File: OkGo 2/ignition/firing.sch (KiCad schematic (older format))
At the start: 62 parts, among them K201 RELAY_SPST, K202 RELAY_SPST, K203 RELAY_SPST, K204 RELAY_SPST, K205 RELAY_SPST, P201 CH1, P202 CH2, P203 CH3, P204 CH4, Q201 BSS138BK, Q202 BSS138BK, Q203 BSS138BK, Q204 BSS138BK, Q205 BSS138BK

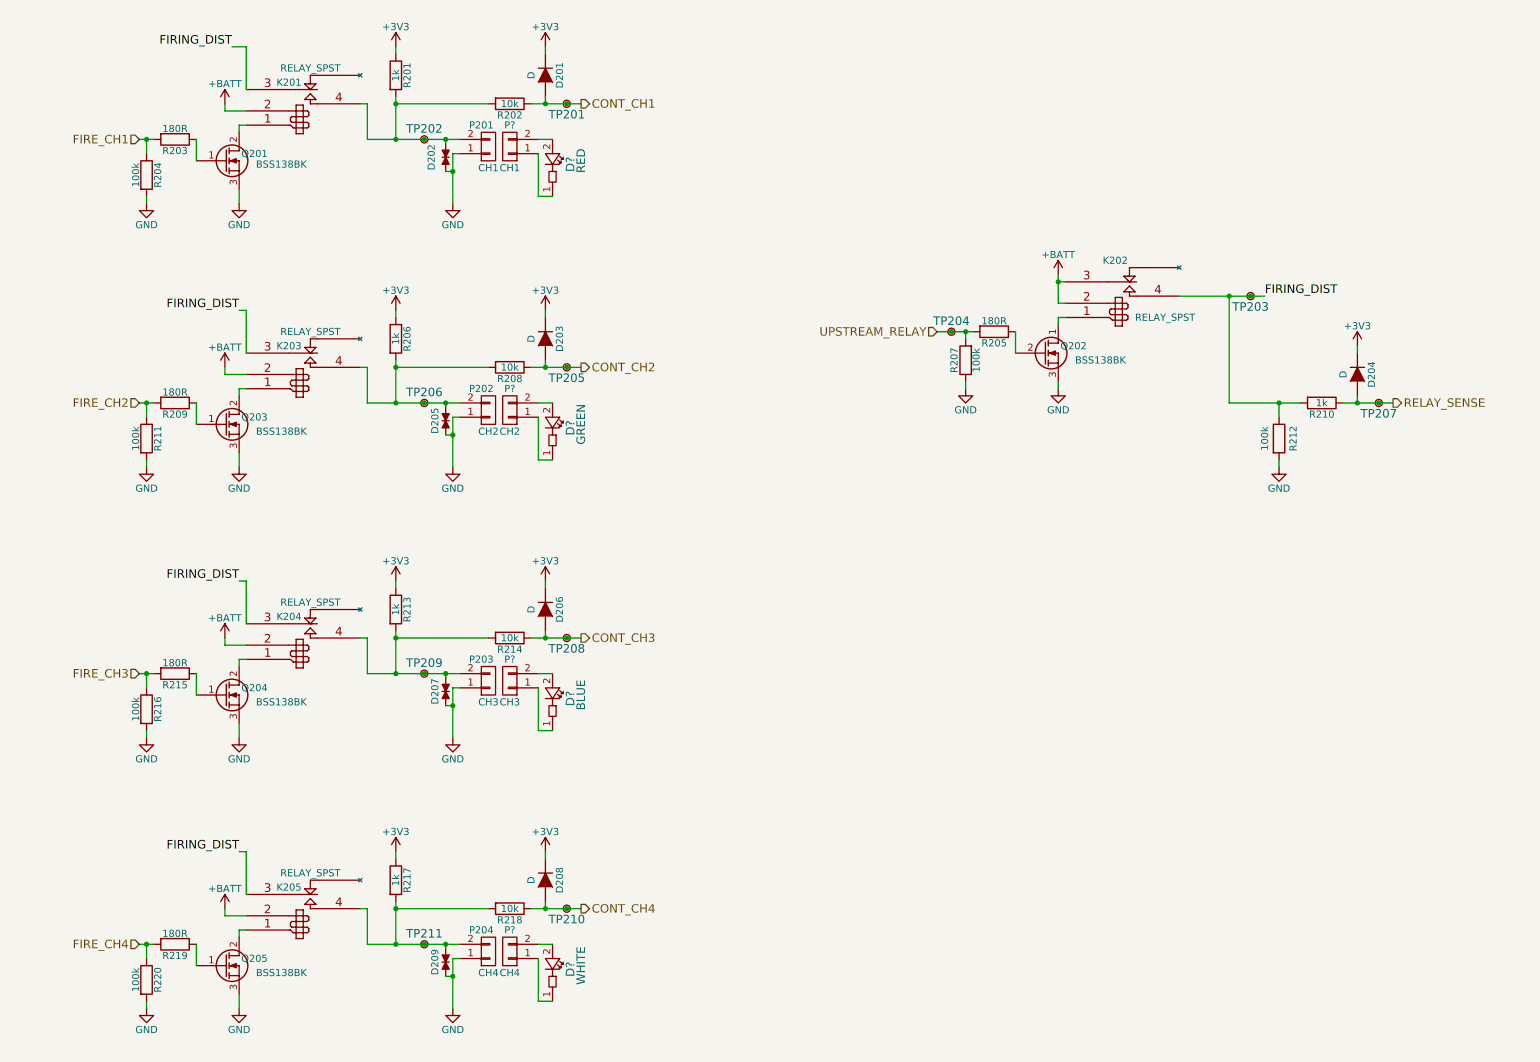
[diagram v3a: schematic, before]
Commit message: New power buttons and arm/disarm LED
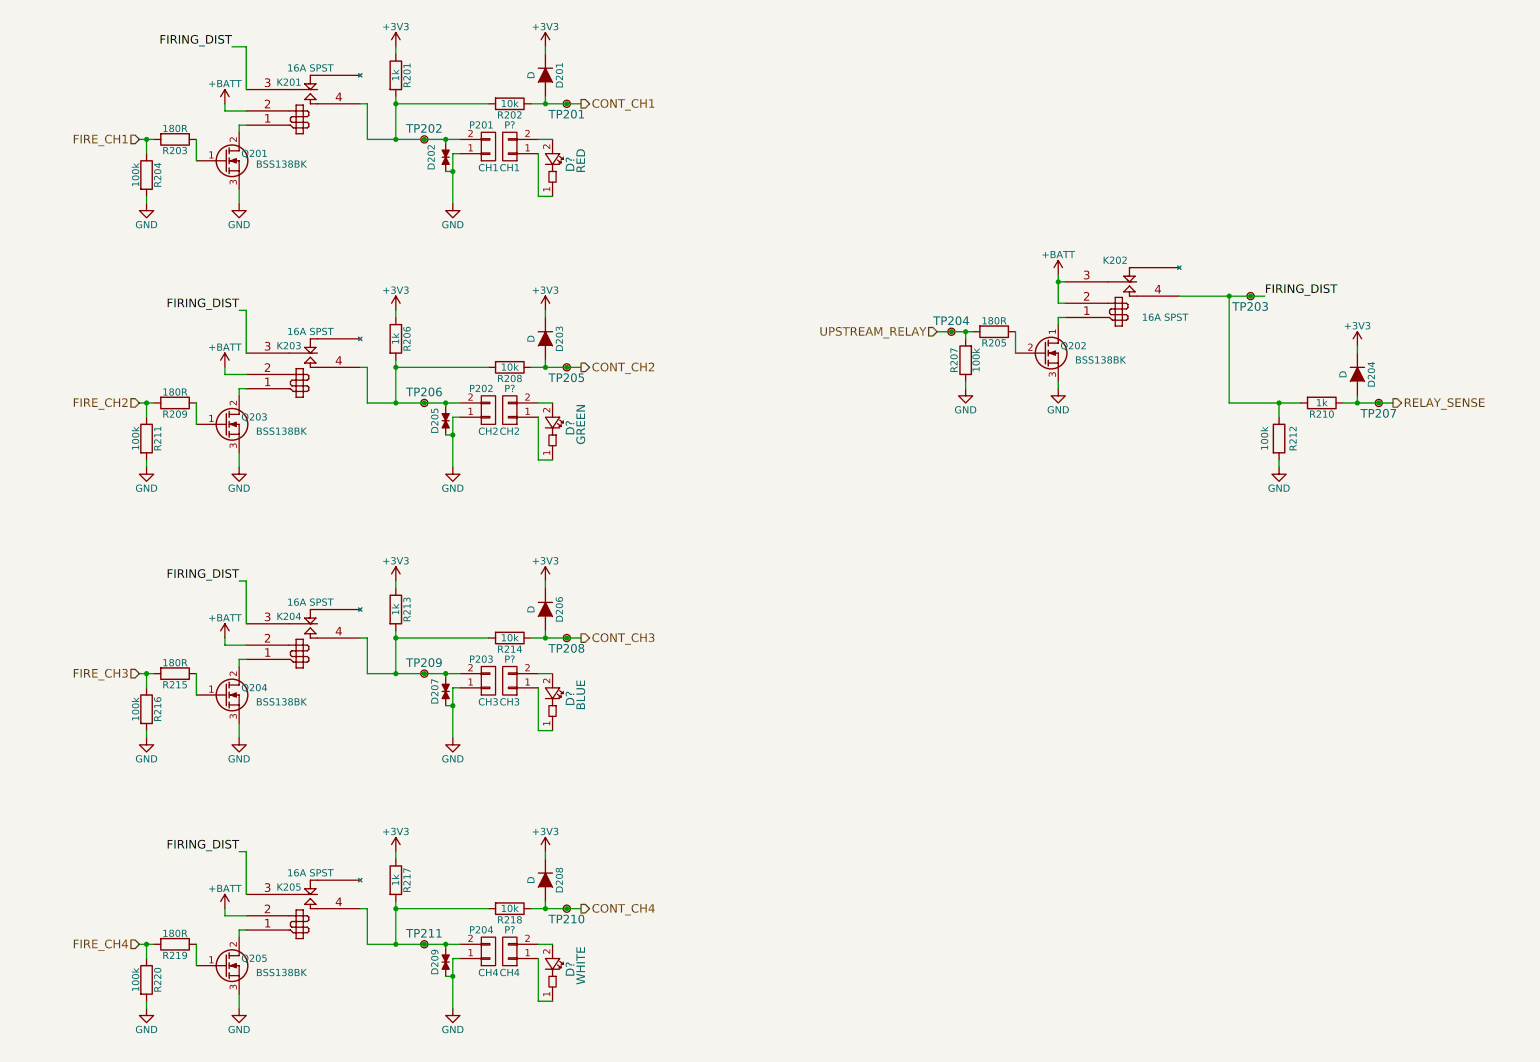
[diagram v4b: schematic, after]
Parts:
- K201, K202, K203, K204, K205: value RELAY_SPST -> 16A SPST
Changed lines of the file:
@@
 LIBS:lipo_3s
 LIBS:spst_small
+LIBS:part
+LIBS:push_illum
+LIBS:push_illum_straight
 LIBS:ignition-cache
 EELAYER 25 0
@@
 P 8300 2650
 F 0 "K202" H 8250 3050 50  0000 C CNN
-F 1 "RELAY_SPST" H 8600 2650 50  0000 C CNN
+F 1 "16A SPST" H 8600 2650 50  0000 C CNN
 F 2 "" H 8300 2650 60  0000 C CNN
 F 3 "" H 8300 2650 60  0000 C CNN
@@
 P 2550 1300
 F 0 "K201" H 2450 1600 50  0000 C CNN
-F 1 "RELAY_SPST" H 2600 1700 50  0000 C CNN
+F 1 "16A SPST" H 2600 1700 50  0000 C CNN
 F 2 "" H 2550 1300 60  0000 C CNN
 F 3 "" H 2550 1300 60  0000 C CNN
@@
 P 2550 3150
 F 0 "K203" H 2450 3450 50  0000 C CNN
-F 1 "RELAY_SPST" H 2600 3550 50  0000 C CNN
+F 1 "16A SPST" H 2600 3550 50  0000 C CNN
 F 2 "" H 2550 3150 60  0000 C CNN
 F 3 "" H 2550 3150 60  0000 C CNN
@@
 P 2550 5050
 F 0 "K204" H 2450 5350 50  0000 C CNN
-F 1 "RELAY_SPST" H 2600 5450 50  0000 C CNN
+F 1 "16A SPST" H 2600 5450 50  0000 C CNN
 F 2 "" H 2550 5050 60  0000 C CNN
 F 3 "" H 2550 5050 60  0000 C CNN
@@
 P 2550 6950
 F 0 "K205" H 2450 7250 50  0000 C CNN
-F 1 "RELAY_SPST" H 2600 7350 50  0000 C CNN
+F 1 "16A SPST" H 2600 7350 50  0000 C CNN
 F 2 "" H 2550 6950 60  0000 C CNN
 F 3 "" H 2550 6950 60  0000 C CNN

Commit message: Changed and moved firing LEDs
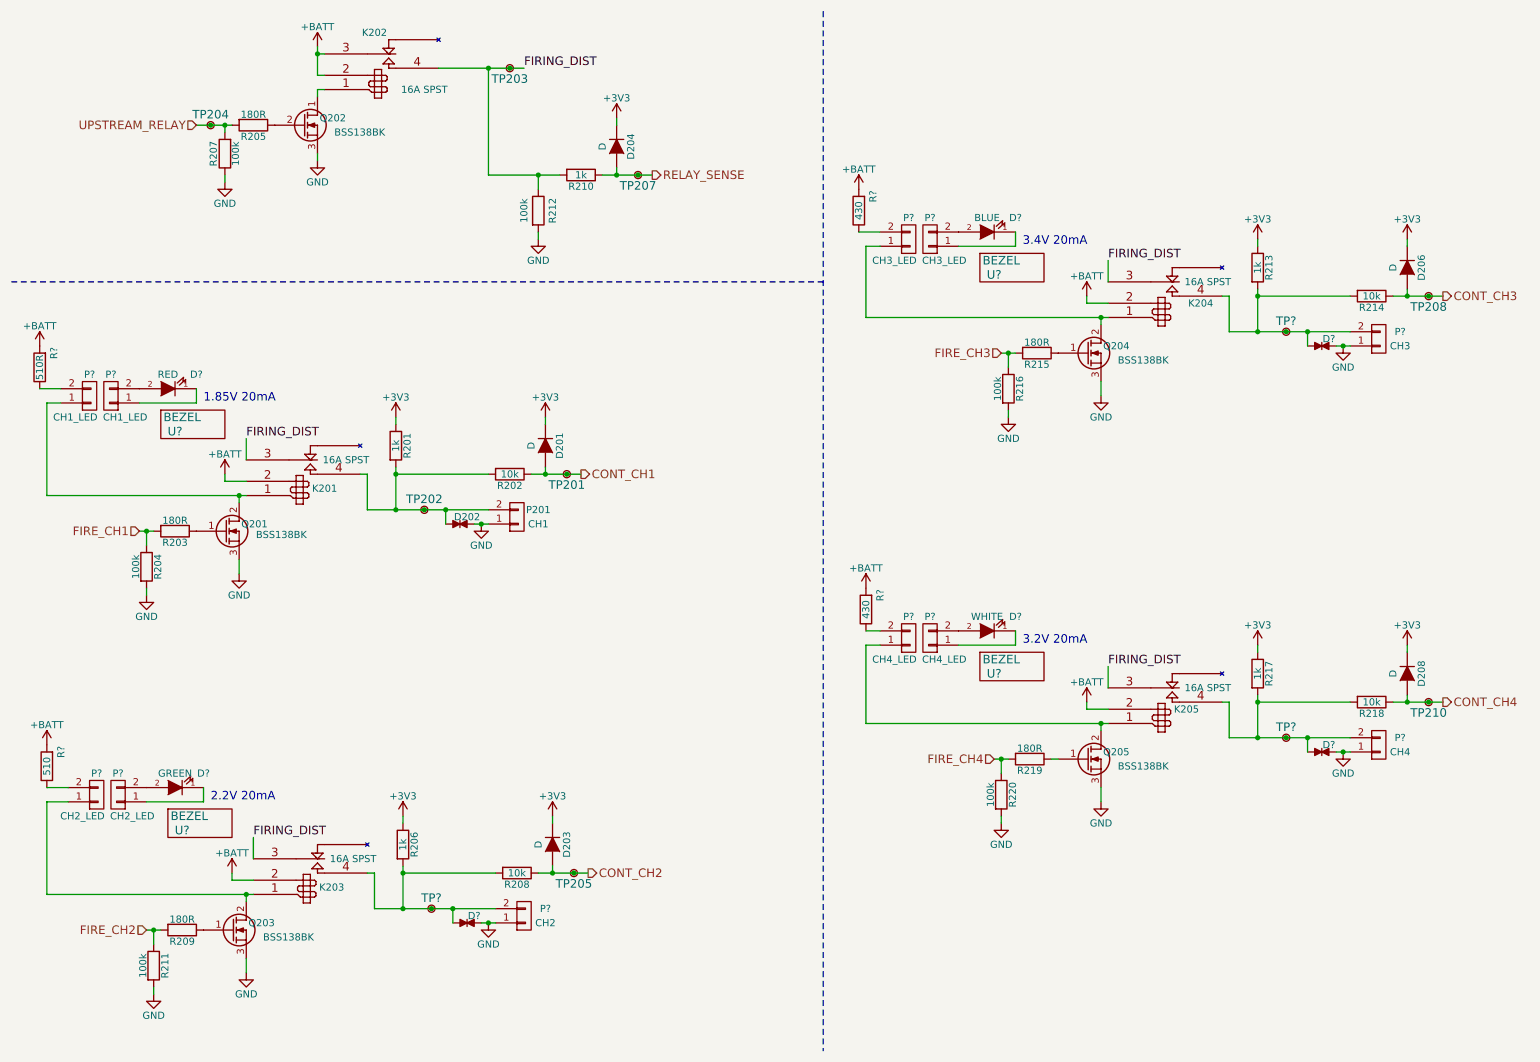
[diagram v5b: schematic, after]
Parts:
- removed D205, D207, D209: TVS_small, Resistors_SMD:R_0603_HandSoldering, symbol TVS_small
- removed D?: RED, symbol LED_R
- removed D?: GREEN, symbol LED_R
- removed D?: BLUE, symbol LED_R
- removed D?: WHITE, symbol LED_R
- removed P202, P?: CH2, symbol CONN_01X02
- removed P203, P?: CH3, symbol CONN_01X02
- removed P204, P?: CH4, symbol CONN_01X02
- removed P?: CH1, symbol CONN_01X02
- removed TP206, TP209, TP211: TestPoint, symbol TestPoint
- added D?: RED, symbol LED
- added D? (x3): TVS_small, Resistors_SMD:R_0603_HandSoldering, symbol TVS_small
- added D?: GREEN, symbol LED
- added D?: BLUE, symbol LED
- added D?: WHITE, symbol LED
- added P? (x2): CH1_LED, symbol CONN_01X02
- added P?: CH2, symbol CONN_01X02
- added P? (x2): CH2_LED, symbol CONN_01X02
- added P?: CH3, symbol CONN_01X02
- added P? (x2): CH3_LED, symbol CONN_01X02
- added P?: CH4, symbol CONN_01X02
- added P? (x2): CH4_LED, symbol CONN_01X02
- added R?: 510R, Resistors_SMD:R_0805_HandSoldering, symbol R
- added R?: 510, Resistors_SMD:R_0805_HandSoldering, symbol R
- added R? (x2): 430, Resistors_SMD:R_0805_HandSoldering, symbol R
- added TP? (x3): TestPoint, symbol TestPoint
- added U? (x4): BEZEL, symbol PART
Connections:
- net +BATT: now also R?.2, R?.2, R?.2, R?.2
- net GND: now also D?.2, D?.2, D?.2, P?.1 (P1), P?.1 (P1), P?.1 (P1)
- net at K203.4, R206.2, R208.2: now also D?.1, P?.2 (P2), TP?.1
- net at K204.4, R213.2, R214.2: now also D?.1, P?.2 (P2), TP?.1
- net at K205.4, R217.2, R218.2: now also D?.1, P?.2 (P2), TP?.1
- net at K201.1, Q201.2 (D): now also P?.1 (P1)
- net at K203.1, Q203.2 (D): now also P?.1 (P1)
- net at K204.1, Q204.2 (D): now also P?.1 (P1)
- net at K205.1, Q205.2 (D): now also P?.1 (P1)
- new net: P?.2 (P2), R?.1 (x4)
- new net: D?.1 (K), P?.1 (P1) (x4)
- new net: D?.2 (A), P?.2 (P2) (x4)
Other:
- note added: "1.85V 20mA"
- note added: "2.2V 20mA"
- note added: "3.2V 20mA"
- note added: "3.4V 20mA"
- moved on the sheet: D201, D202, D203, D204, D206, D208, K201, K202, K203, K204, K205, P201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

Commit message: Lots of footprinting.
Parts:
- gave numbers to parts that had none: 29
- renumbered D204 to D201, D206 to D203, D201 to D206, D202 to D207, D208 to D209, D203 to D212, K202 to K201, K204 to K202, K201 to K203, K205 to K204, K203 to K205, P201 to P206, Q202 to Q201, Q204 to Q202, Q201 to Q203, Q205 to Q204, Q203 to Q205, R205 to R201, R207 to R202, R210 to R203, R212 to R204, R213 to R206, R214 to R207, R215 to R208, R216 to R210, R201 to R211, R202 to R212, R203 to R213, R204 to R214, R217 to R216, R218 to R217, R219 to R218, R206 to R221, R208 to R222, R209 to R223, R211 to R224, TP203 to TP201, TP204 to TP202, TP207 to TP203, TP208 to TP204, TP201 to TP206, TP202 to TP207, TP210 to TP208, TP205 to TP210

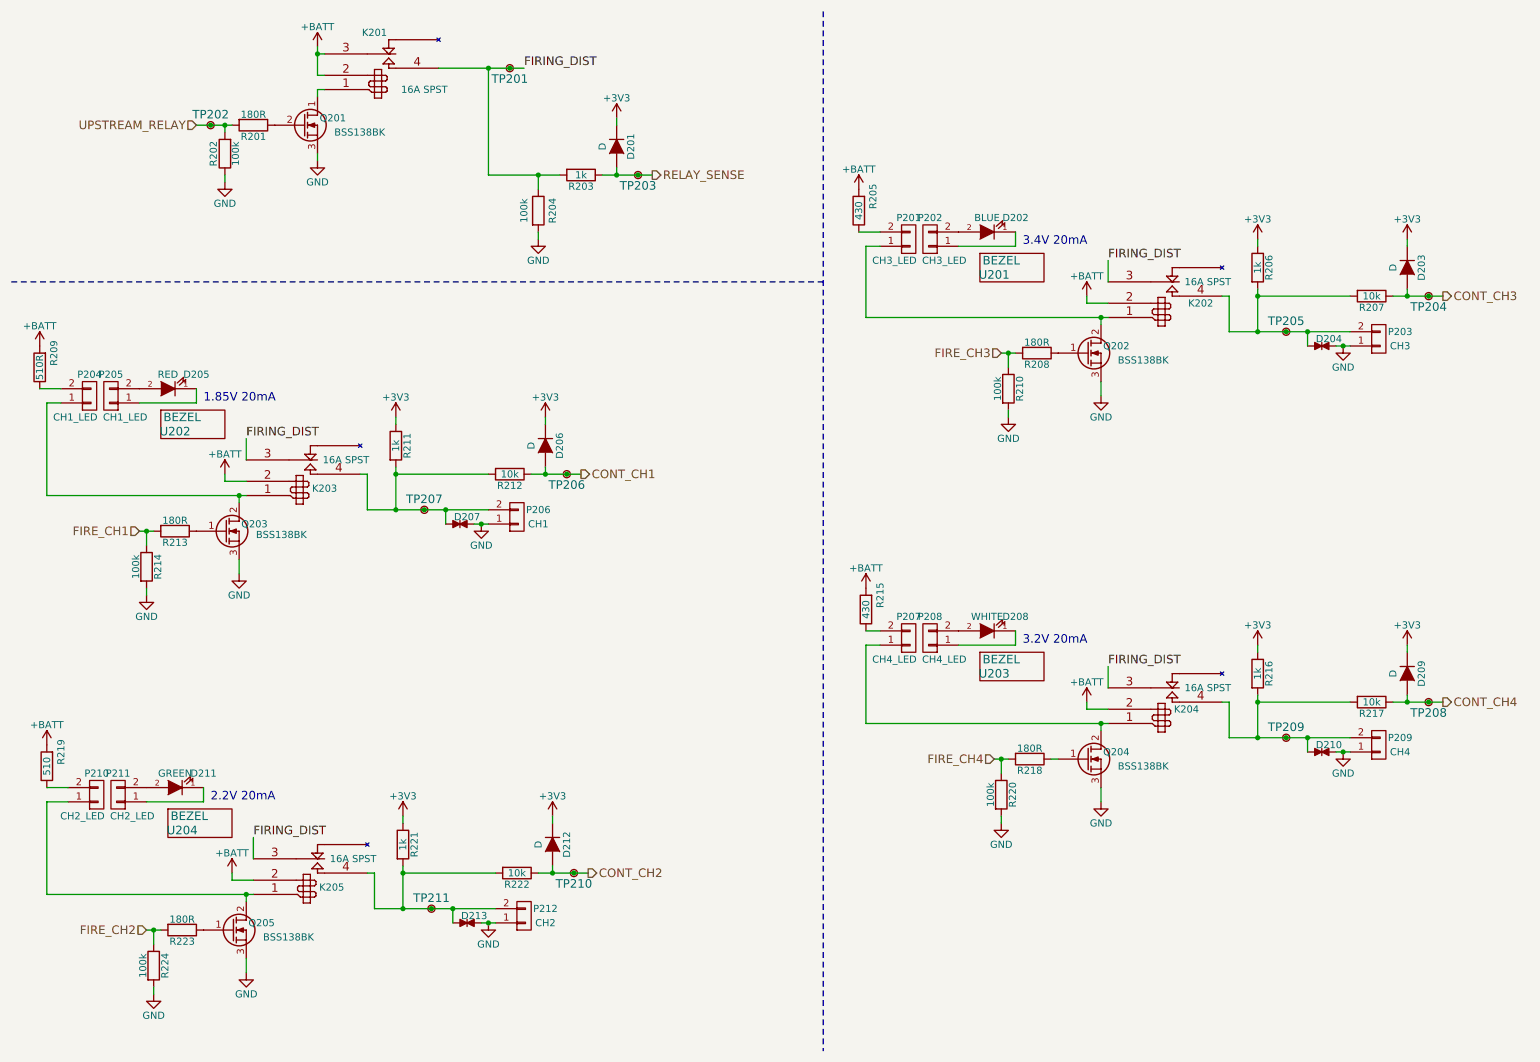
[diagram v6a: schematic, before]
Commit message: Footprinting on ignition + TPs
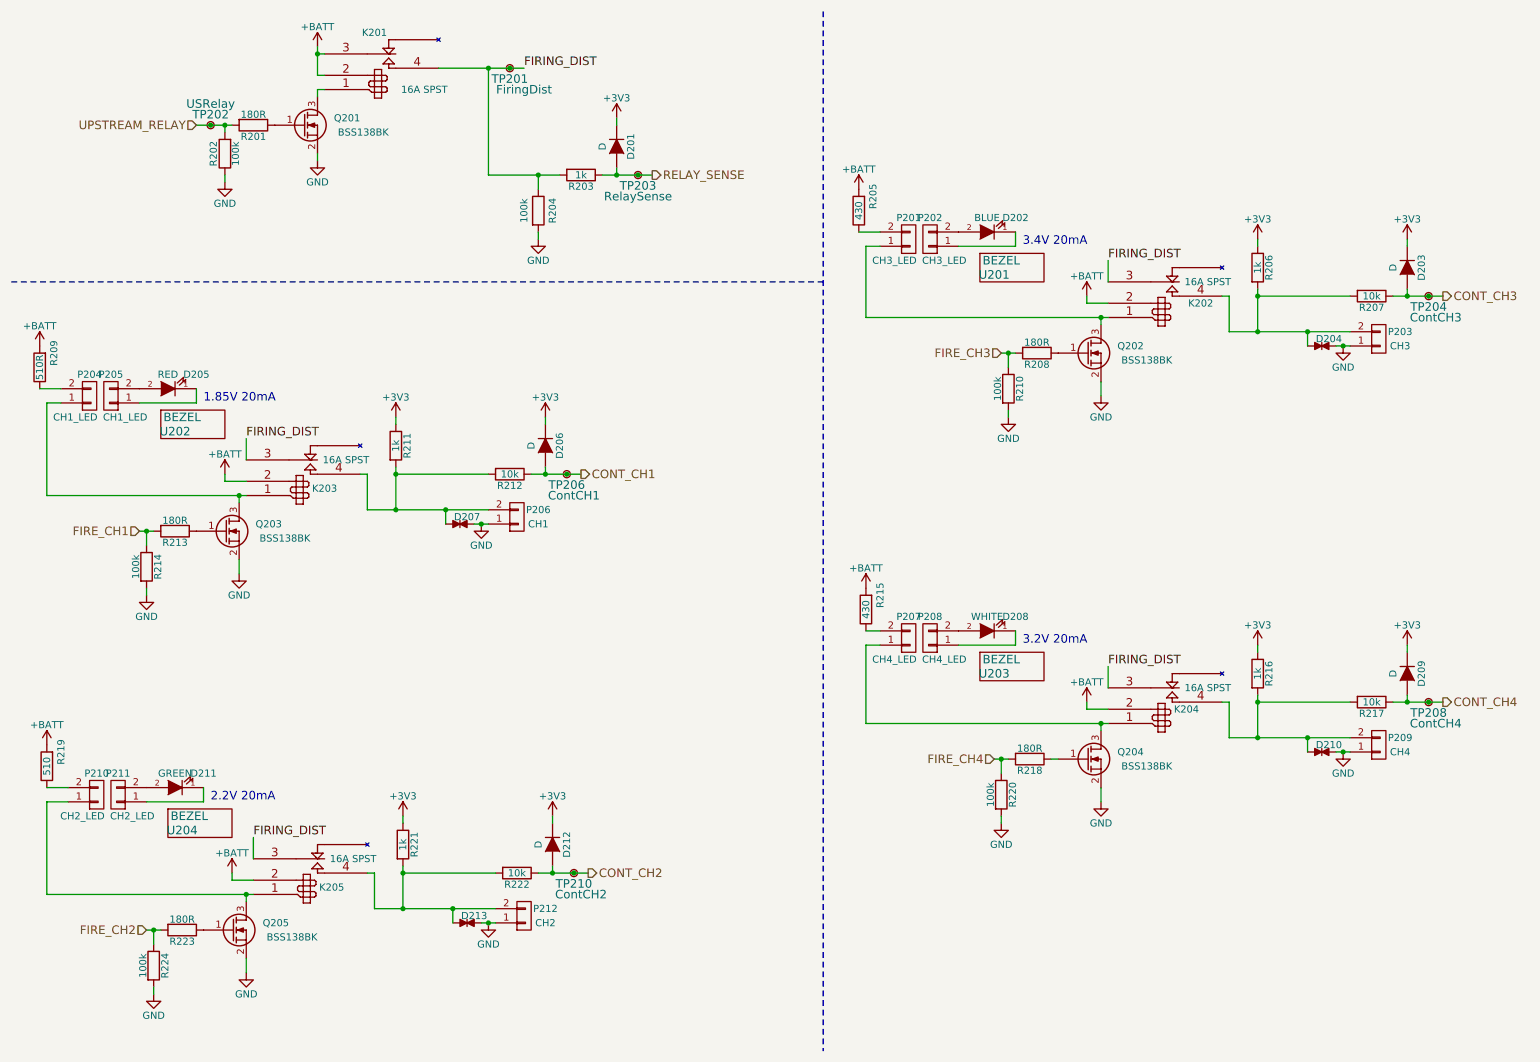
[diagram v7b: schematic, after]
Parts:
- removed Q201: BSS138BK, symbol Q_NMOS_DGS
- removed Q202, Q203, Q204, Q205: BSS138BK, symbol Q_NMOS_GDS-RESCUE-ignition
- removed TP205, TP207, TP209, TP211: TestPoint, symbol TestPoint
- added Q201, Q203, Q204, Q205: BSS138BK, Housings_SOT-23_SOT-143_TSOT-6:SOT-23, symbol Q_NMOS_GSD
- added Q202: BSS138BK, symbol Q_NMOS_GSD
- TP201: value TestPoint -> FiringDist; footprint (none) -> common:TESTPOINT
- TP202: value TestPoint -> USRelay; footprint (none) -> common:TESTPOINT
- TP203: value TestPoint -> RelaySense; footprint (none) -> common:TESTPOINT
- TP204: value TestPoint -> ContCH3; footprint (none) -> common:TESTPOINT
- TP206: value TestPoint -> ContCH1; footprint (none) -> common:TESTPOINT
- TP208: value TestPoint -> ContCH4; footprint (none) -> common:TESTPOINT
- TP210: value TestPoint -> ContCH2; footprint (none) -> common:TESTPOINT
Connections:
- net GND: now also Q201.2 (S), Q202.2 (S), Q203.2 (S), Q204.2 (S), Q205.2 (S)
- net at K201.1: now also Q201.3 (D)
- net at R201.1: now also Q201.1 (G)
- net at K203.1, P204.1 (P1): now also Q203.3 (D)
- net at R213.1: now also Q203.1 (G)
- net at K205.1, P210.1 (P1): now also Q205.3 (D)
- net at R223.1: now also Q205.1 (G)
- net at K202.1, P201.1 (P1): now also Q202.3 (D)
- net at R208.1: now also Q202.1 (G)
- net at K204.1, P207.1 (P1): now also Q204.3 (D)
- net at R218.1: now also Q204.1 (G)
